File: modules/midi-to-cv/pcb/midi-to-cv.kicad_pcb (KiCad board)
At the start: 2 copper layers, 38.2 x 110.1 mm, 48 parts, among them J1 MIDI in, J2 DEBUG HEADER, J3 CV1, J4 CV2, J5 CV3, J6 CV4, J7 GATE1, J8 GATE2, J9 Conn_02x08_Odd_Even, U1 6N137, U2 ATtiny4313-PU, U3 MCP4822, U4 MCP4822, U5 LM324, Y1 20mhz

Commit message: modules: midi-to-cv: fix references
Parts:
- D2: value LED -> LED Red
- D3, D4: value LED -> LED Green
- J1: value MIDI in -> Thonkiconn ST
- J2: value DEBUG HEADER -> JST XH 1x2
- J3: value CV1 -> Thonkiconn SM
- J4: value CV2 -> Thonkiconn SM
- J5: value CV3 -> Thonkiconn SM
- J6: value CV4 -> Thonkiconn SM
- J7: value GATE1 -> Thonkiconn SM
- J8: value GATE2 -> Thonkiconn SM
- J9: value Conn_02x08_Odd_Even -> IDC Header 2x8
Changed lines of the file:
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@@
   (page A4)
   (title_block
-    (title "midi-to-cv board")
+    (title midi-to-cv)
     (date 2021-12-15)
     (rev 1.0)
@@
       (effects (font (size 1 1) (thickness 0.15)) (justify mirror))
     )
-    (fp_text value Conn_02x08_Odd_Even (at 1.27 -23.88) (layer B.Fab)
+    (fp_text value "IDC Header 2x8" (at 1.27 -23.88) (layer B.Fab)
       (effects (font (size 1 1) (thickness 0.15)) (justify mirror))
     )
@@
       (effects (font (size 1 1) (thickness 0.15)) (justify mirror))
     )
-    (fp_text value "DEBUG HEADER" (at 1.25 -4.6 270) (layer B.Fab)
+    (fp_text value "JST XH 1x2" (at 1.25 -4.6 270) (layer B.Fab)
       (effects (font (size 1 1) (thickness 0.15)) (justify mirror))
     )
@@
       (effects (font (size 1 1) (thickness 0.15)))
     )
-    (fp_text value LED (at 1.4732 2.96) (layer F.Fab)
+    (fp_text value "LED Green" (at 1.4732 2.96) (layer F.Fab)
       (effects (font (size 1 1) (thickness 0.15)))
     )
@@
       (effects (font (size 1 1) (thickness 0.15)))
     )
-    (fp_text value LED (at 1.4732 2.96) (layer F.Fab)
+    (fp_text value "LED Green" (at 1.4732 2.96) (layer F.Fab)
       (effects (font (size 1 1) (thickness 0.15)))
     )
@@
       (effects (font (size 1 1) (thickness 0.15)))
     )
-    (fp_text value LED (at 1.4732 2.96 90) (layer F.Fab)
+    (fp_text value "LED Red" (at 1.4732 2.96 90) (layer F.Fab)
       (effects (font (size 1 1) (thickness 0.15)))
     )
@@
       (effects (font (size 1 1) (thickness 0.15)))
     )
-    (fp_text value "MIDI in" (at 0 -5) (layer F.Fab)
+    (fp_text value "Thonkiconn ST" (at 0 -5) (layer F.Fab)
       (effects (font (size 1 1) (thickness 0.15)))
     )
@@
       (effects (font (size 1 1) (thickness 0.15)))
     )
-    (fp_text value GATE2 (at 0 -5) (layer F.Fab)
+    (fp_text value "Thonkiconn SM" (at 0 -5) (layer F.Fab)
       (effects (font (size 1 1) (thickness 0.15)))
     )
@@
       (effects (font (size 1 1) (thickness 0.15)))
     )
-    (fp_text value GATE1 (at 0 -5) (layer F.Fab)
+    (fp_text value "Thonkiconn SM" (at 0 -5) (layer F.Fab)
       (effects (font (size 1 1) (thickness 0.15)))
     )
@@
       (effects (font (size 1 1) (thickness 0.15)))
     )
-    (fp_text value CV4 (at 0 -5) (layer F.Fab)
+    (fp_text value "Thonkiconn SM" (at 0 -5) (layer F.Fab)
       (effects (font (size 1 1) (thickness 0.15)))
     )
@@
       (effects (font (size 1 1) (thickness 0.15)))
     )
-    (fp_text value CV3 (at 0 -5) (layer F.Fab)
+    (fp_text value "Thonkiconn SM" (at 0 -5) (layer F.Fab)
       (effects (font (size 1 1) (thickness 0.15)))
     )
@@
       (effects (font (size 1 1) (thickness 0.15)))
     )
-    (fp_text value CV2 (at 0 -5) (layer F.Fab)
+    (fp_text value "Thonkiconn SM" (at 0 -5) (layer F.Fab)
       (effects (font (size 1 1) (thickness 0.15)))
     )
@@
       (effects (font (size 1 1) (thickness 0.15)))
     )
-    (fp_text value CV1 (at 0 -5) (layer F.Fab)
-      (effects (font (size 1 1) (thickness 0.15)))
-    )
+    (fp_text value "Thonkiconn SM" (at 0 -5) (layer F.Fab)
+      (effects (font (size 1 1) (thickness 0.15)))
+    )

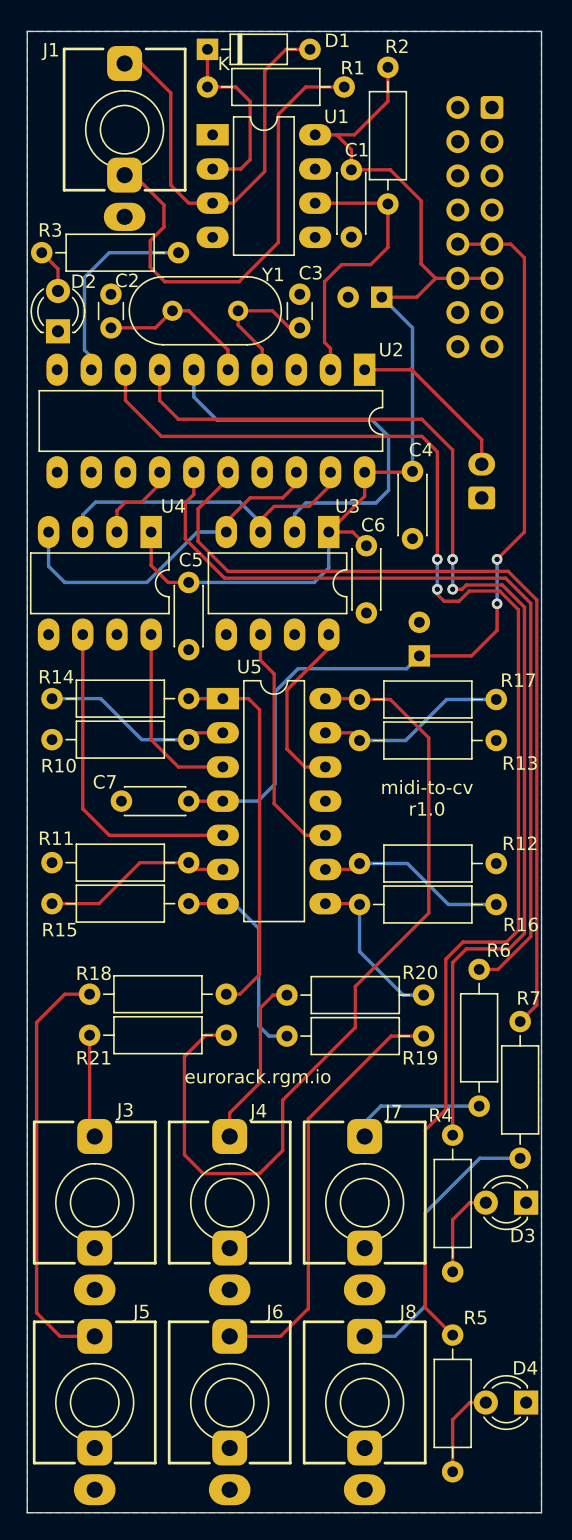
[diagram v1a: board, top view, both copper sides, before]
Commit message: modules: midi-to-cv: upgrade to kicad 6
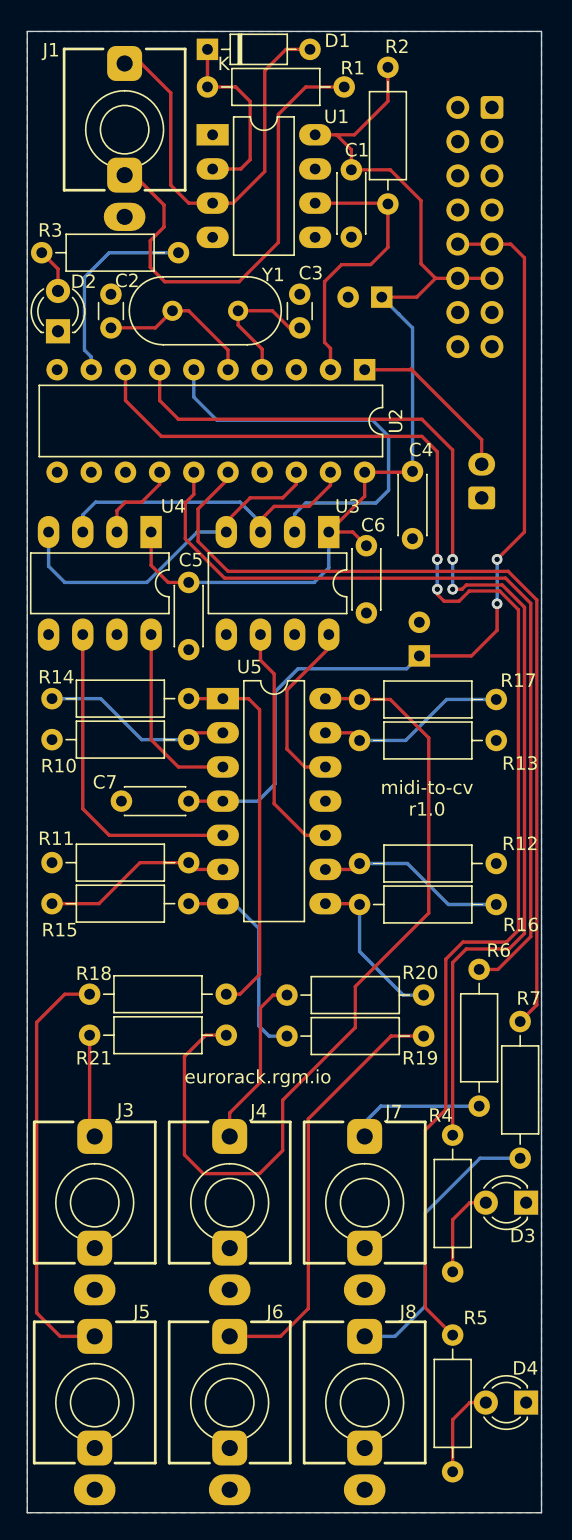
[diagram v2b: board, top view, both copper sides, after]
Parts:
- U2: footprint Package_DIP:DIP-20_W7.62mm_LongPads -> Package_DIP:DIP-20_W7.62mm
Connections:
- J1 pad S: (no net) -> unconnected-(J1-PadS)
- J3 pad TN: (no net) -> unconnected-(J3-PadTN)
- J4 pad TN: (no net) -> unconnected-(J4-PadTN)
- J5 pad TN: (no net) -> unconnected-(J5-PadTN)
- J6 pad TN: (no net) -> unconnected-(J6-PadTN)
- J7 pad TN: (no net) -> unconnected-(J7-PadTN)
- J8 pad TN: (no net) -> unconnected-(J8-PadTN)
- J9 pad 1: (no net) -> unconnected-(J9-Pad1)
- J9 pad 13: (no net) -> unconnected-(J9-Pad13)
- J9 pad 14: (no net) -> unconnected-(J9-Pad14)
- J9 pad 15: (no net) -> unconnected-(J9-Pad15)
- J9 pad 16: (no net) -> unconnected-(J9-Pad16)
- J9 pad 2: (no net) -> unconnected-(J9-Pad2)
- U1 pad 1: (no net) -> unconnected-(U1-Pad1)
- U1 pad 7: (no net) -> unconnected-(U1-Pad7)
- U2 pad 11: (no net) -> unconnected-(U2-Pad11)
- U2 pad 12: (no net) -> unconnected-(U2-Pad12)
- U2 pad 13: (no net) -> unconnected-(U2-Pad13)
- U2 pad 17: (no net) -> unconnected-(U2-Pad17)
- U2 pad 3: (no net) -> unconnected-(U2-Pad3)
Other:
- net class Default removed

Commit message: modules: midi-to-cv: revision A (redesign)
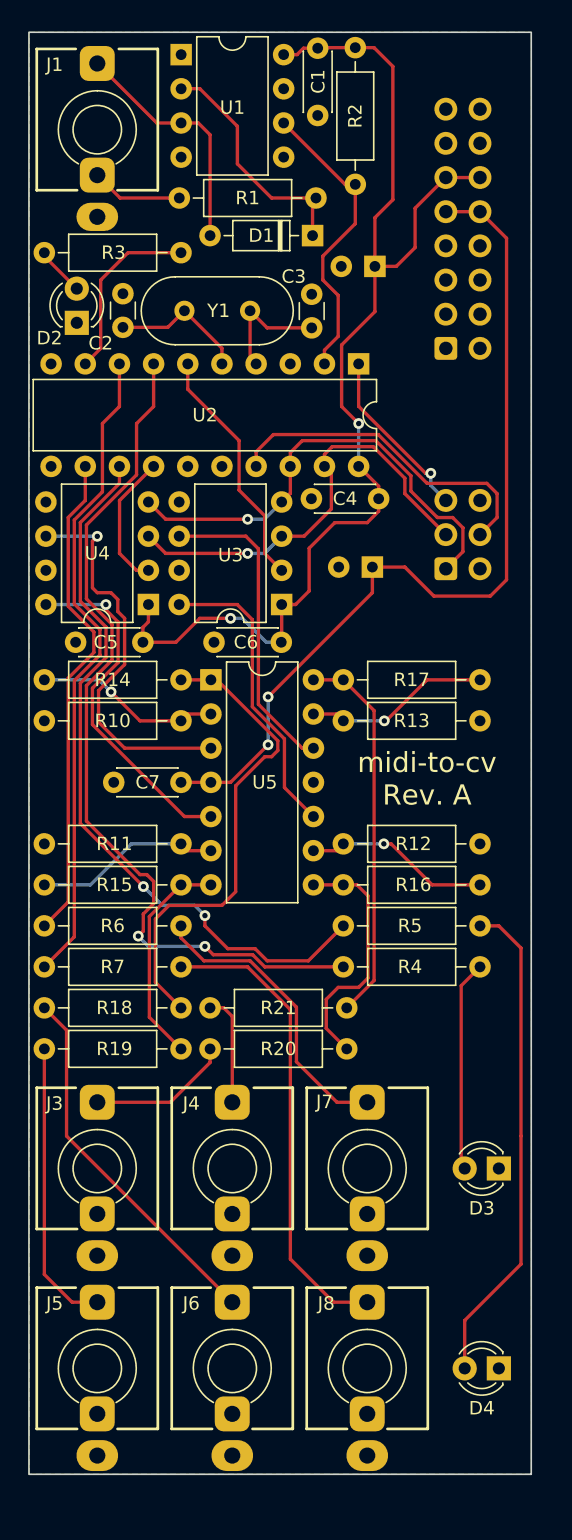
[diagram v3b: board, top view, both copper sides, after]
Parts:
- added REF**: Eurorack_PCB_8HP, eurorack:Eurorack_PCB_8HP, F.Cu at (151.4, 95.4)
- D2, D3, D4: footprint eurorack:LED_D3.0mmP2.54mm -> LED_THT:LED_D3.0mm
- J2: value JST XH 1x2 -> ISP; footprint Connector_JST:JST_XH_B2B-XH-A_1x02_P2.50mm_Vertical -> eurorack:IDC-Header_2x03_P2.54mm_Vertical
- J9: value IDC Header 2x8 -> Eurorack PSU; footprint Connector_IDC:IDC-Header_2x08_P2.54mm_Vertical -> eurorack:IDC-Header_2x08_P2.54mm_Vertical
- U1, U3, U4: footprint Package_DIP:DIP-8_W7.62mm_LongPads -> Package_DIP:DIP-8_W7.62mm
- U5: footprint Package_DIP:DIP-14_W7.62mm_LongPads -> Package_DIP:DIP-14_W7.62mm
- Y1: value 20mhz -> 20MHz
- moved R7 35.6 mm to (133.9, 111.3), turned to 0 degrees
- moved R6 32.5 mm to (133.9, 108.2), turned to 0 degrees
- moved R5 31.5 mm to (156.1, 108.2), turned to 0 degrees
- moved R19 28.2 mm to (133.9, 117.3), turned to 0 degrees
- moved REF** 21.4 mm to (162.9, 116.5)
- moved J9 18.2 mm to (163.7, 65.3), turned to 0 degrees
- moved D1 15.9 mm to (153.8, 56.9), turned to 180 degrees
- moved R4 14.9 mm to (156.1, 111.3), turned to 0 degrees
- moved R1 11.5 mm to (154.1, 54.1), turned to 180 degrees
- moved C6 9.57 mm to (151.5, 87.1), turned to 180 degrees
- moved C1 9.38 mm to (154.2, 43.0)
- moved R21 9.18 mm to (146.2, 114.3)
- moved C9 7.47 mm to (158.2, 81.5), turned to 180 degrees
- moved R20 6.98 mm to (146.2, 117.3)
- moved U3 6.43 mm to (151.5, 84.3), turned to 180 degrees
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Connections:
- J2 pad 1: GND -> SPI_SD
- J2 pad 2: dw -> unconnected-(J2-Pad2)
- R18 pad 1: CV3 -> CV4
- R19 pad 1: CV4 -> CV3
- R20 pad 1: CV2 -> CV1
- R21 pad 1: CV1 -> CV2
- U2 pad 1: dw -> RESET
- U2 pad 12: unconnected-(U2-Pad12) -> GATE1
- U2 pad 13: unconnected-(U2-Pad13) -> LED3
- U2 pad 15: GATE1 -> unconnected-(U2-Pad15)
- U2 pad 16: GATE2 -> unconnected-(U2-Pad16)
- U2 pad 17: unconnected-(U2-Pad17) -> ISP_MOSI
- U2 pad 8: LED3 -> GATE2
- U5 pad 10: DAC_CV2 -> DAC_CV1
- U5 pad 12: DAC_CV1 -> DAC_CV2
- U5 pad 3: DAC_CV3 -> DAC_CV4
- U5 pad 5: DAC_CV4 -> DAC_CV3
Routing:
- net LED3: track 104.3 -> 54.6 mm
- net Net-(R17-Pad1): track 63.7 -> 28.4 mm
- net Net-(D4-Pad2): track 6.86 -> 36.7 mm
- net Net-(J1-PadR): track 35.3 -> 6.80 mm
- net GATE1: track 62.5 -> 37.0 mm
- net ISP_MOSI: track 0.00 -> 24.9 mm
- net LED2: track 85.4 -> 65.2 mm
- net GATE2: track 64.9 -> 48.7 mm
- net Net-(J8-PadT): track 21.1 -> 35.0 mm
- net SPI_CS1: track 31.9 -> 18.2 mm
- net Net-(D1-Pad2): track 31.2 -> 18.1 mm
- net RESET: track 0.00 -> 13.1 mm, vias 0 -> 1
- net dw: track 12.7 -> 0.00 mm
- net DAC_CV3: track 14.0 -> 26.2 mm, vias 0 -> 1
- net Net-(J7-PadT): track 10.1 -> 22.2 mm
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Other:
- board size 38.2 x 110.1 mm -> 37.3 x 107.2 mm
- board text added: "midi-to-cv Rev. A"
- board text removed: "midi-to-cv r1.0"
